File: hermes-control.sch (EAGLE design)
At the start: 76 parts, among them J1 1981568-1, J3 2201778-1, Q1 MMBT2222A, Q2 BC849SMD, Q3 FDN360P, Q4 FDN360P, Q5 BC849SMD, Q6 MMBT3906SOT23-3, Q7 FDN360P, Q8 MMBT2222A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

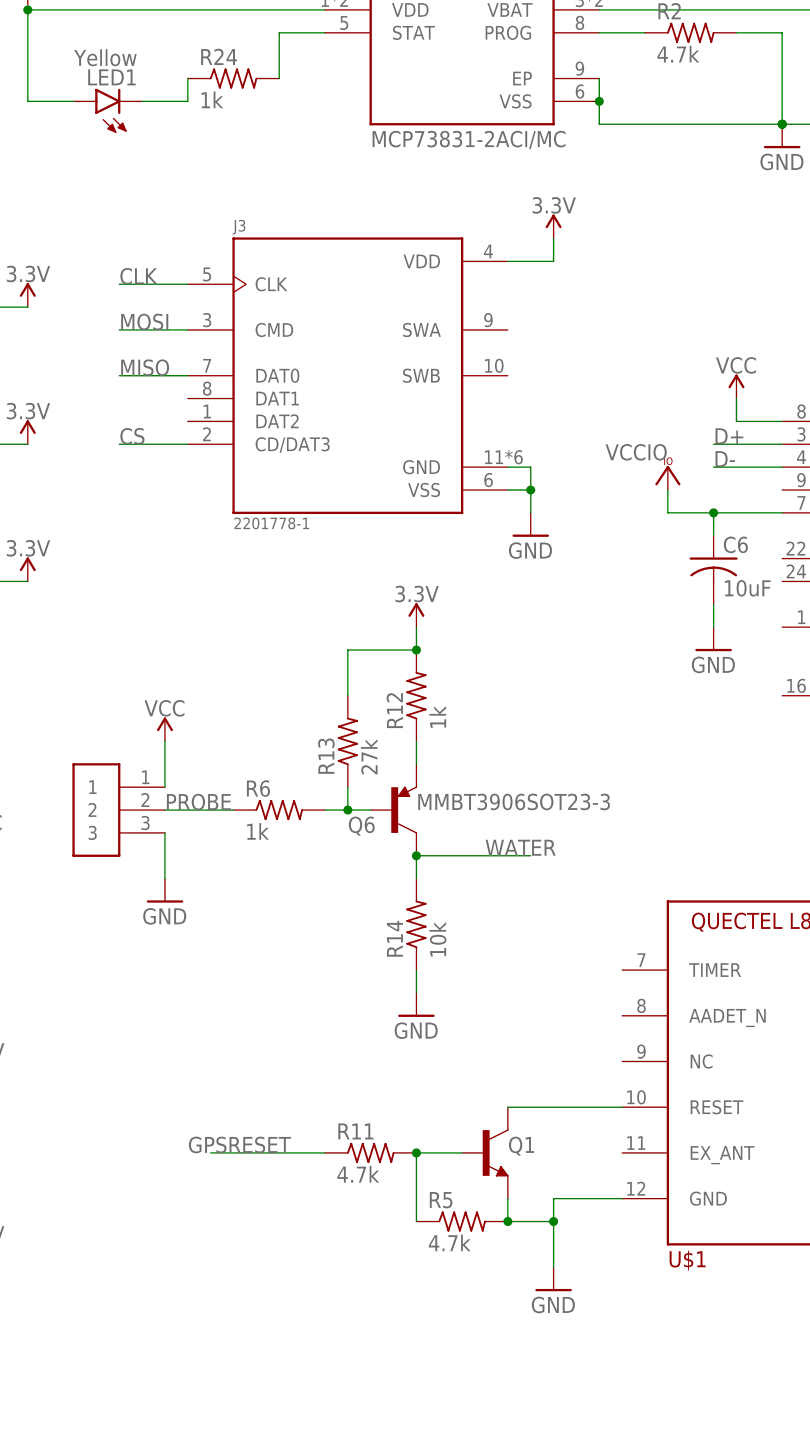
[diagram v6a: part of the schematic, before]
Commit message: almost everything is connected
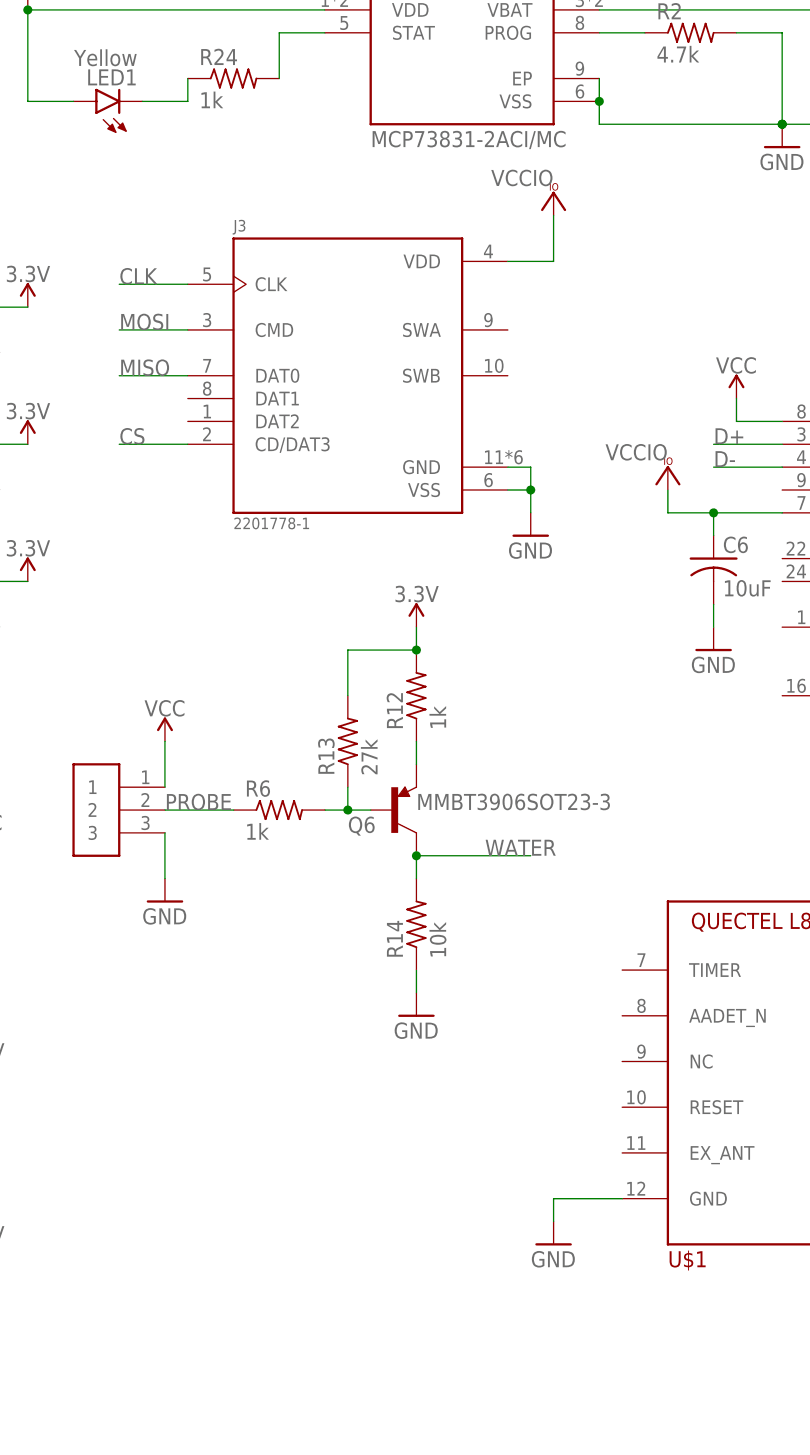
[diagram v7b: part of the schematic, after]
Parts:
- removed Q1: MMBT2222A, hermes:MMBT2222A
- removed R11, R5: 4.7k, rcl:R-US_R0603
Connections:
- removed net GPSRESET: R11.1
- removed net N$12: Q1.C, U$1.RESET
- removed net N$8: Q1.B, R11.2, R5.1
- net 3.3V: no longer J3.VDD
- net GND: no longer Q1.E, R5.2
- net VCCIO: now also J3.VDD
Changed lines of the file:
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@@
 <part name="GND9" library="supply1" library_urn="urn:adsk.eagle:library:371" deviceset="GND" device=""/>
 <part name="GND10" library="supply1" library_urn="urn:adsk.eagle:library:371" deviceset="GND" device=""/>
-<part name="Q1" library="hermes" deviceset="MMBT2222A" device="" value="MMBT2222A"/>
 <part name="SUPPLY13" library="SparkFun-PowerSymbols" library_urn="urn:adsk.eagle:library:530" deviceset="V_BATT" device=""/>
 <part name="GND14" library="supply1" library_urn="urn:adsk.eagle:library:371" deviceset="GND" device=""/>
@@
 <part name="U1" library="hermes-parts" deviceset="LSM9DS1TR" device=""/>
 <part name="J3" library="hermes" deviceset="2201778-1" device=""/>
-<part name="SUPPLY12" library="SparkFun-PowerSymbols" library_urn="urn:adsk.eagle:library:530" deviceset="3.3V" device=""/>
 <part name="GND13" library="supply1" library_urn="urn:adsk.eagle:library:371" deviceset="GND" device=""/>
 <part name="LBAT" library="hermes" deviceset="S2B-PH-SM4-TB(LF)(SN)" device=""/>
@@
 <part name="C5" library="rcl" library_urn="urn:adsk.eagle:library:334" deviceset="C-US" device="C0603" package3d_urn="urn:adsk.eagle:package:23616/2" value="0.1uF"/>
 <part name="C8" library="rcl" library_urn="urn:adsk.eagle:library:334" deviceset="C-US" device="C0603" package3d_urn="urn:adsk.eagle:package:23616/2" value="4.7uF"/>
-<part name="R11" library="rcl" library_urn="urn:adsk.eagle:library:334" deviceset="R-US_" device="R0603" package3d_urn="urn:adsk.eagle:package:23555/3" value="4.7k"/>
-<part name="R5" library="rcl" library_urn="urn:adsk.eagle:library:334" deviceset="R-US_" device="R0603" package3d_urn="urn:adsk.eagle:package:23555/3" value="4.7k"/>
 <part name="C6" library="rcl" library_urn="urn:adsk.eagle:library:334" deviceset="C-US" device="C0603" package3d_urn="urn:adsk.eagle:package:23616/2" value="10uF"/>
 <part name="SUPPLY9" library="SparkFun-PowerSymbols" library_urn="urn:adsk.eagle:library:530" deviceset="VCC" device=""/>
@@
 <part name="VCC4" library="supply1" library_urn="urn:adsk.eagle:library:371" deviceset="VCCIO" device=""/>
 <part name="VCC5" library="supply1" library_urn="urn:adsk.eagle:library:371" deviceset="VCCIO" device=""/>
+<part name="VCC6" library="supply1" library_urn="urn:adsk.eagle:library:371" deviceset="VCCIO" device=""/>
 </parts>
 <sheets>
@@
 <attribute name="VALUE" x="226.06" y="40.64" size="1.778" layer="96"/>
 </instance>
-<instance part="GND10" gate="1" x="129.54" y="25.4" smashed="yes">
-<attribute name="VALUE" x="127" y="22.86" size="1.778" layer="96"/>
-</instance>
-<instance part="Q1" gate="&gt;NAME" x="121.92" y="40.64" smashed="yes">
-<attribute name="NAME" x="124.46" y="40.64" size="1.778" layer="95" font="vector"/>
+<instance part="GND10" gate="1" x="129.54" y="30.48" smashed="yes">
+<attribute name="VALUE" x="127" y="27.94" size="1.778" layer="96"/>
 </instance>
 <instance part="SUPPLY13" gate="G$1" x="337.82" y="99.06" smashed="yes">
@@
 <attribute name="VALUE" x="93.9579" y="109.9524" size="1.272209375" layer="96"/>
 </instance>
-<instance part="SUPPLY12" gate="G$1" x="129.54" y="142.24" smashed="yes">
-<attribute name="VALUE" x="129.54" y="145.034" size="1.778" layer="96" align="bottom-center"/>
-</instance>
 <instance part="GND13" gate="1" x="127" y="109.22" smashed="yes">
 <attribute name="VALUE" x="124.46" y="106.68" size="1.778" layer="96"/>
@@
 <attribute name="NAME" x="206.756" y="61.595" size="1.778" layer="95"/>
 <attribute name="VALUE" x="206.756" y="56.769" size="1.778" layer="96"/>
-</instance>
-<instance part="R11" gate="G$1" x="109.22" y="40.64" smashed="yes">
-<attribute name="NAME" x="105.41" y="42.1386" size="1.778" layer="95"/>
-<attribute name="VALUE" x="105.41" y="37.338" size="1.778" layer="96"/>
-</instance>
-<instance part="R5" gate="G$1" x="119.38" y="33.02" smashed="yes">
-<attribute name="NAME" x="115.57" y="34.5186" size="1.778" layer="95"/>
-<attribute name="VALUE" x="115.57" y="29.718" size="1.778" layer="96"/>
 </instance>
 <instance part="C6" gate="G$1" x="147.32" y="106.68" smashed="yes">
@@
 <instance part="VCC5" gate="G$1" x="142.24" y="116.84" smashed="yes">
 <attribute name="VALUE" x="142.24" y="119.38" size="1.778" layer="96" rot="R180"/>
+</instance>
+<instance part="VCC6" gate="G$1" x="129.54" y="147.32" smashed="yes">
+<attribute name="VALUE" x="129.54" y="149.86" size="1.778" layer="96" rot="R180"/>
 </instance>
 </instances>
@@
 </segment>
 <segment>
-<pinref part="U$1" gate="G$1" pin="GND@2"/>
-<wire x1="137.16" y1="35.56" x2="129.54" y2="35.56" width="0.1524" layer="91"/>
-<pinref part="GND10" gate="1" pin="GND"/>
-<wire x1="129.54" y1="35.56" x2="129.54" y2="33.02" width="0.1524" layer="91"/>
-<pinref part="Q1" gate="&gt;NAME" pin="E"/>
-<wire x1="129.54" y1="33.02" x2="129.54" y2="27.94" width="0.1524" layer="91"/>
-<wire x1="124.46" y1="33.02" x2="124.46" y2="35.56" width="0.1524" layer="91"/>
-<wire x1="124.46" y1="33.02" x2="129.54" y2="33.02" width="0.1524" layer="91"/>
-<junction x="129.54" y="33.02"/>
-<pinref part="R5" gate="G$1" pin="2"/>
-<junction x="124.46" y="33.02"/>
-</segment>
-<segment>
 <pinref part="GND14" gate="1" pin="GND"/>
 <wire x1="337.82" y1="73.66" x2="337.82" y2="76.2" width="0.1524" layer="91"/>
@@
 <wire x1="355.6" y1="27.94" x2="355.6" y2="30.48" width="0.1524" layer="91"/>
 </segment>
+<segment>
+<pinref part="GND10" gate="1" pin="GND"/>
+<wire x1="129.54" y1="33.02" x2="129.54" y2="35.56" width="0.1524" layer="91"/>
+<pinref part="U$1" gate="G$1" pin="GND@2"/>
+<wire x1="129.54" y1="35.56" x2="137.16" y2="35.56" width="0.1524" layer="91"/>
+</segment>
 </net>
 <net name="N$1" class="0">
@@
 <pinref part="SUPPLY21" gate="G$1" pin="3.3V"/>
 <wire x1="55.88" y1="27.94" x2="66.04" y2="27.94" width="0.1524" layer="91"/>
-</segment>
-<segment>
-<pinref part="J3" gate="G$1" pin="VDD"/>
-<wire x1="124.46" y1="139.7" x2="129.54" y2="139.7" width="0.1524" layer="91"/>
-<pinref part="SUPPLY12" gate="G$1" pin="3.3V"/>
-<wire x1="129.54" y1="139.7" x2="129.54" y2="142.24" width="0.1524" layer="91"/>
 </segment>
 <segment>
@@
 </segment>
 </net>
-<net name="N$12" class="0">
-<segment>
-<pinref part="Q1" gate="&gt;NAME" pin="C"/>
-<pinref part="U$1" gate="G$1" pin="RESET"/>
-<wire x1="124.46" y1="45.72" x2="137.16" y2="45.72" width="0.1524" layer="91"/>
-</segment>
-</net>
-<net name="GPSRESET" class="0">
-<segment>
-<wire x1="104.14" y1="40.64" x2="91.44" y2="40.64" width="0.1524" layer="91"/>
-<label x="88.9" y="40.64" size="1.778" layer="95"/>
-<pinref part="R11" gate="G$1" pin="1"/>
-</segment>
-</net>
 <net name="IO13" class="0">
 <segment>
@@
 <wire x1="238.76" y1="119.38" x2="243.84" y2="119.38" width="0.1524" layer="91"/>
 <pinref part="Q5" gate="G$1" pin="B"/>
-</segment>
-</net>
-<net name="N$8" class="0">
-<segment>
-<pinref part="R5" gate="G$1" pin="1"/>
-<pinref part="R11" gate="G$1" pin="2"/>
-<wire x1="114.3" y1="33.02" x2="114.3" y2="40.64" width="0.1524" layer="91"/>
-<pinref part="Q1" gate="&gt;NAME" pin="B"/>
-<wire x1="114.3" y1="40.64" x2="119.38" y2="40.64" width="0.1524" layer="91"/>
-<junction x="114.3" y="40.64"/>
 </segment>
 </net>
@@
 <pinref part="VCC5" gate="G$1" pin="VCCIO"/>
 </segment>
-</net>
+<segment>
+<pinref part="J3" gate="G$1" pin="VDD"/>
+<pinref part="VCC6" gate="G$1" pin="VCCIO"/>
+<wire x1="129.54" y1="144.78" x2="129.54" y2="139.7" width="0.1524" layer="91"/>
+<wire x1="129.54" y1="139.7" x2="124.46" y2="139.7" width="0.1524" layer="91"/>
+</segment>
+</net>

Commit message: flip sd card and connect vcc to usb uart chip
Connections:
- removed net N$11: U3.VBUS
- net VCC: now also U3.VBUS
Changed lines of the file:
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@@
 <wire x1="332.74" y1="53.34" x2="337.82" y2="53.34" width="0.1524" layer="91"/>
+</segment>
+<segment>
+<pinref part="U3" gate="G$1" pin="VBUS"/>
+<wire x1="154.94" y1="121.92" x2="149.86" y2="121.92" width="0.1524" layer="91"/>
+<pinref part="SUPPLY9" gate="G$1" pin="VCC"/>
+<wire x1="149.86" y1="121.92" x2="149.86" y2="124.46" width="0.1524" layer="91"/>
 </segment>
 </net>
@@
 </segment>
 </net>
-<net name="N$11" class="0">
-<segment>
-<pinref part="U3" gate="G$1" pin="VBUS"/>
-<wire x1="149.86" y1="121.92" x2="154.94" y2="121.92" width="0.1524" layer="91"/>
-<wire x1="149.86" y1="124.46" x2="149.86" y2="121.92" width="0.1524" layer="91"/>
-<pinref part="SUPPLY9" gate="G$1" pin="VCC"/>
-</segment>
-</net>
